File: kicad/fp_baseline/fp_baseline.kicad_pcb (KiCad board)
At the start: 2 copper layers, 95 x 24.7 mm, 1 part, among them J1 JS220

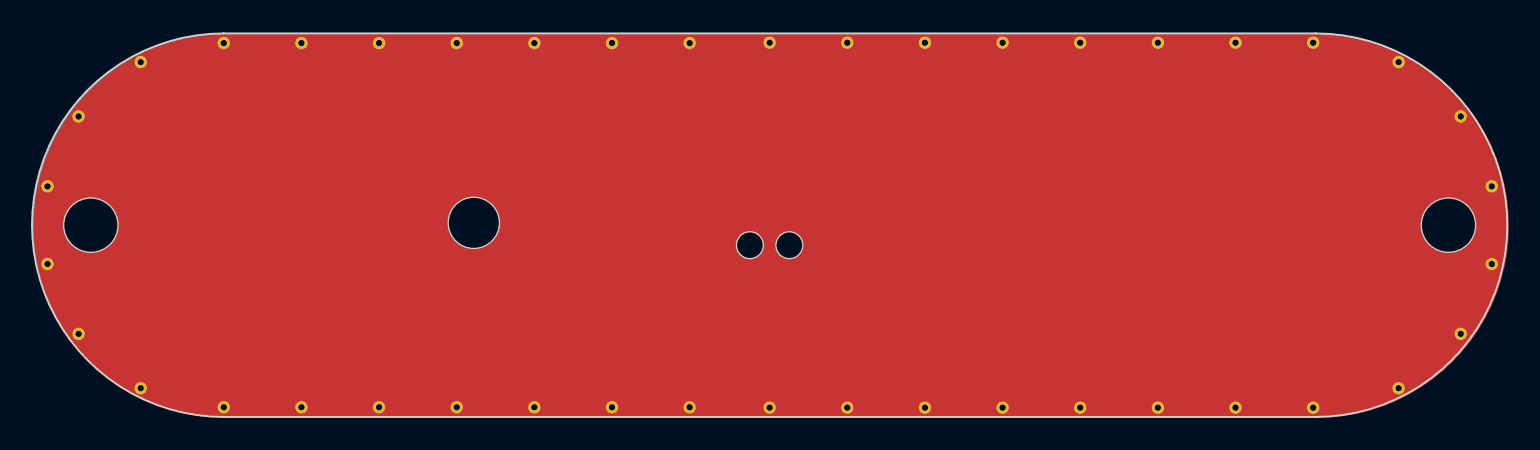
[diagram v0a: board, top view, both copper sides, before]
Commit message: fix front copper polygon so it acts as prper copper pour around pads
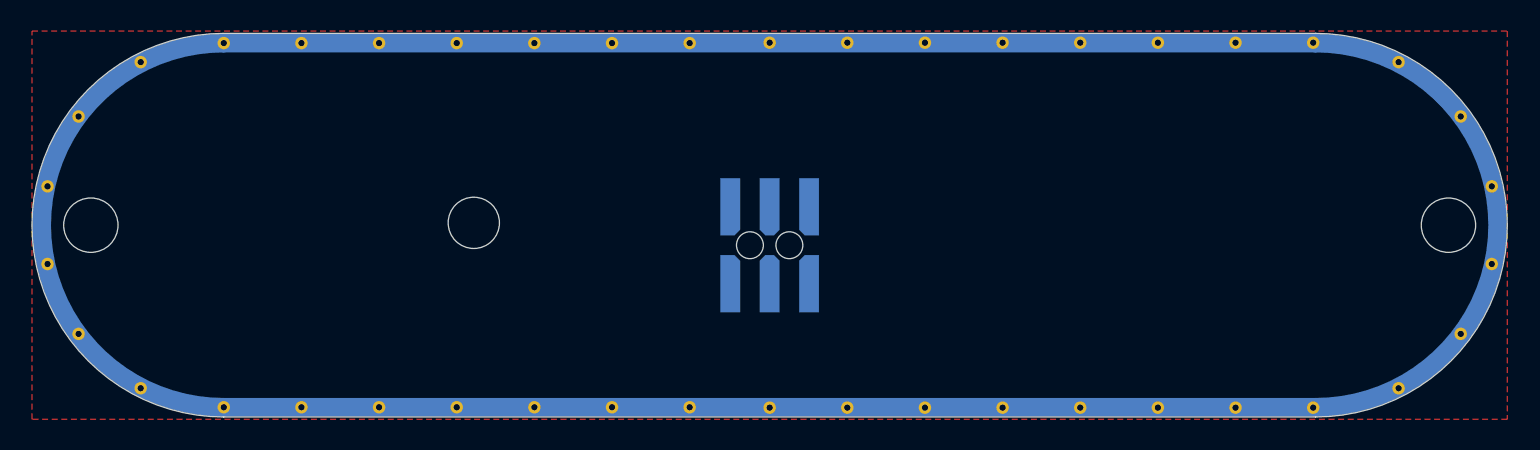
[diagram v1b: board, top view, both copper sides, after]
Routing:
- added copper zone on F.Cu, net GND
